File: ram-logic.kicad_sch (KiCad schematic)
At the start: 17 parts, among them SW1 Button, SW202 Programming Switch, U26 74HCT00, U31 74HCT157

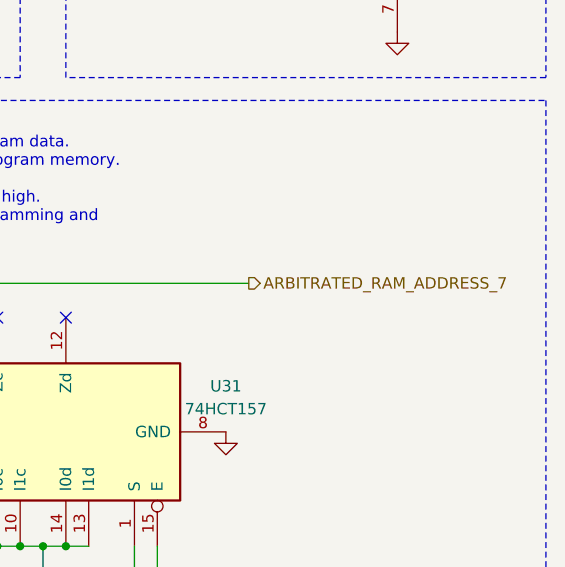
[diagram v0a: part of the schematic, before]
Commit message: ram address 7 led now uses the arbitrated signal
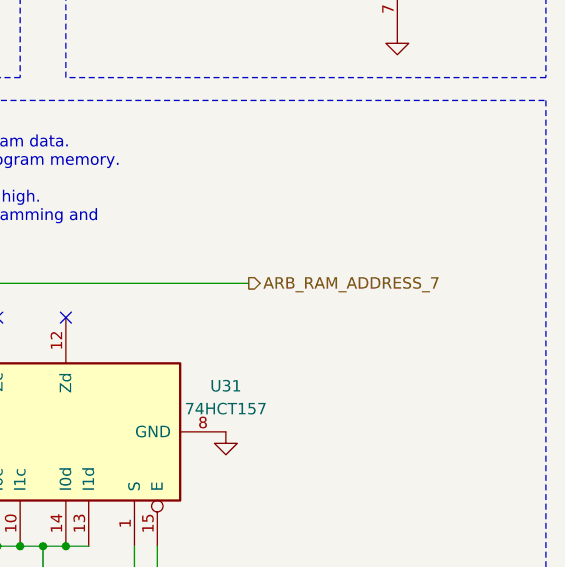
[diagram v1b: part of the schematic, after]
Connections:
- net ARBITRATED_RAM_ADDRESS_7 renamed ARB_RAM_ADDRESS_7
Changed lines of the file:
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@@
     (effects (font (size 1.27 1.27)) (justify left))
   )
-  (hierarchical_label "ARBITRATED_RAM_ADDRESS_7" (shape output) (at 246.38 77.47 0) (fields_autoplaced)
+  (hierarchical_label "ARB_RAM_ADDRESS_7" (shape output) (at 246.38 77.47 0) (fields_autoplaced)
     (effects (font (size 1.27 1.27)) (justify left))
   )

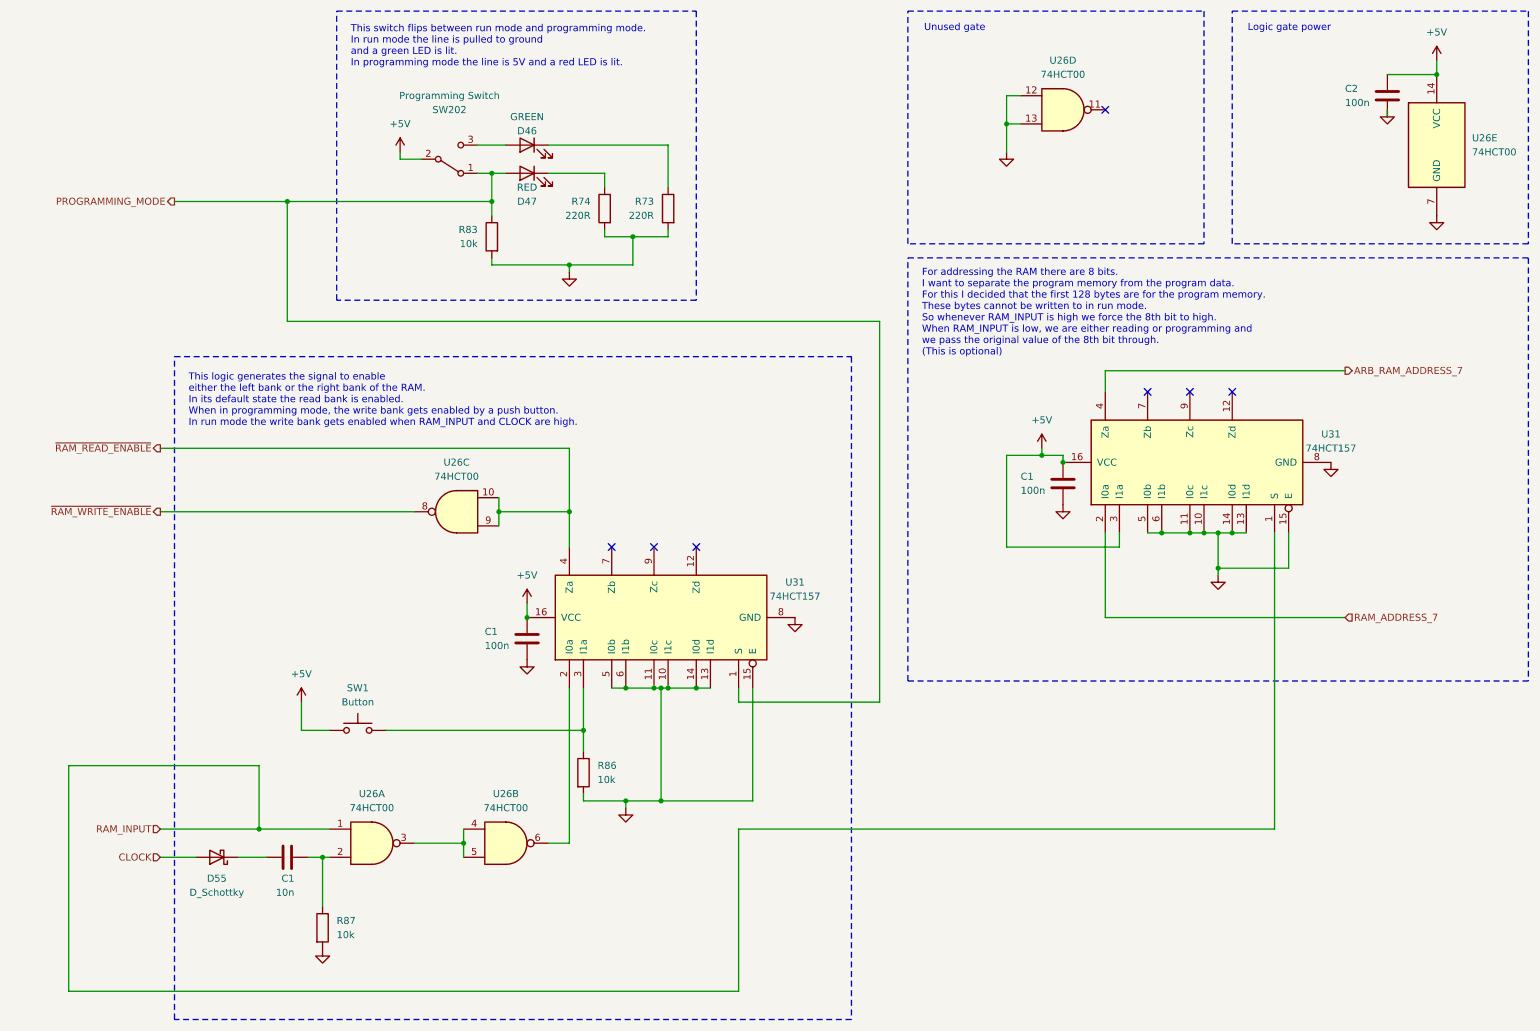
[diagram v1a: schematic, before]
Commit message: added stack and x register.  Added logic for stack_address so ram address 7 gets passes and ram address 8 is high
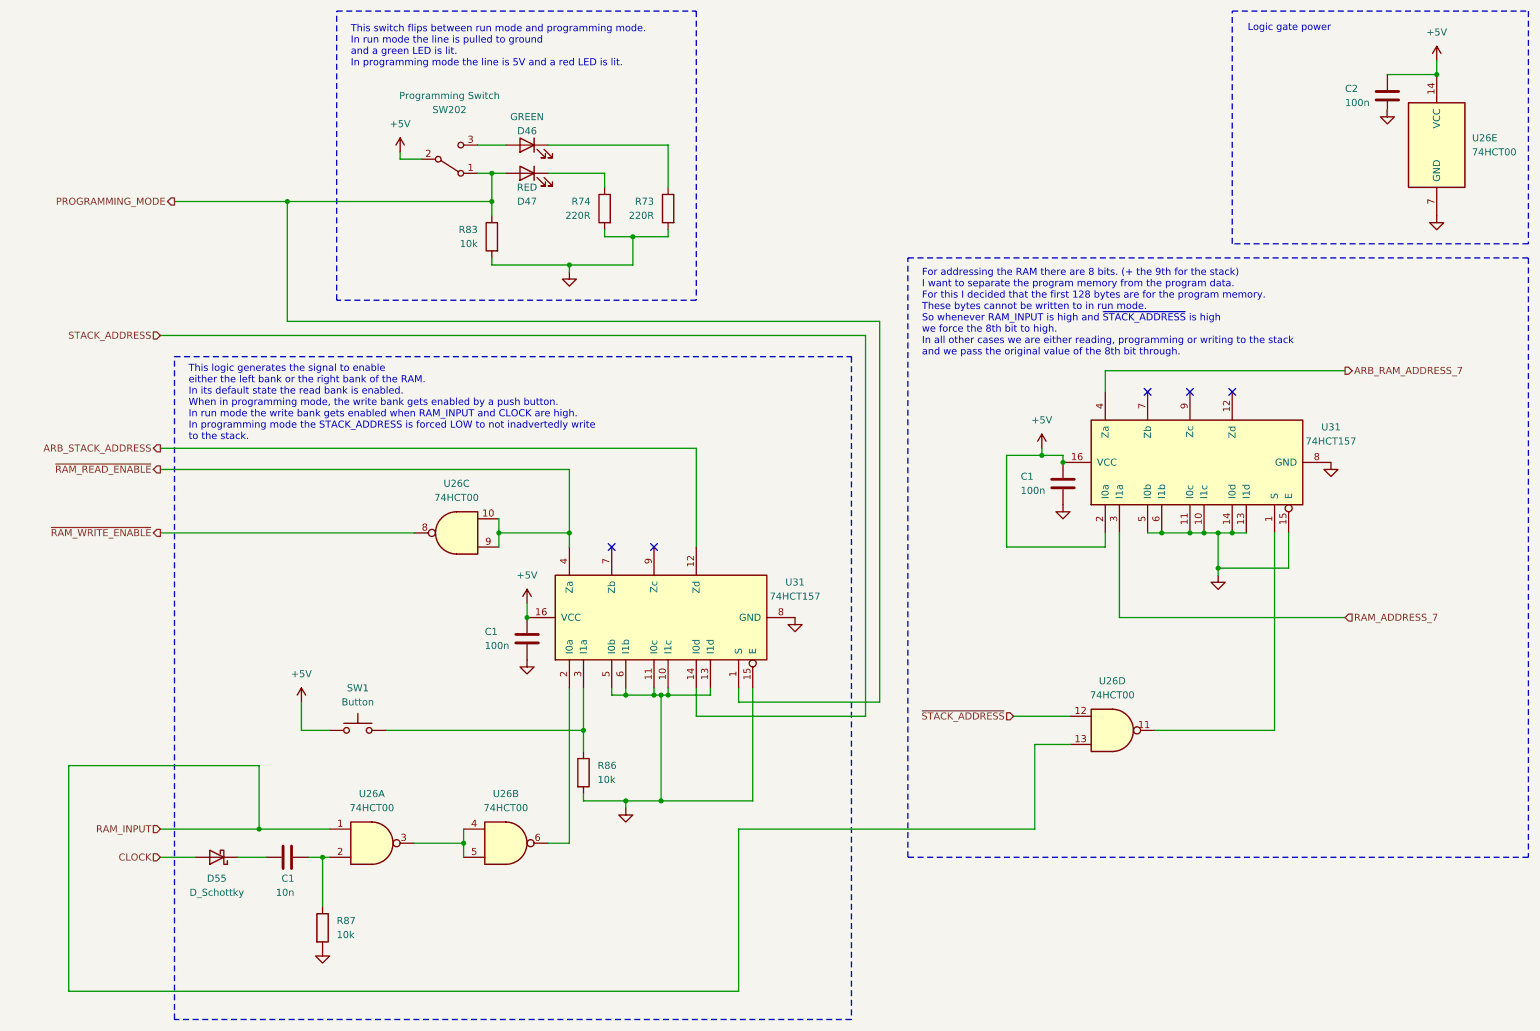
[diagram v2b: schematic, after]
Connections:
- net +5V: now also U31.2 (I0a); no longer U31.3 (I1a)
- net GND: no longer U26.12, U26.13, U31.14 (I0d)
- net RAM_ADDRESS_7: now also U31.3 (I1a); no longer U31.2 (I0a)
- net RAM_INPUT: now also U26.13; no longer U31.1 (S)
- net at U26.11: now also U31.1 (S)
- net ARB_STACK_ADDRESS: now reaches U31.12 (Zd)
- new net STACK_ADDRESS: U31.14 (I0d)
- new net ~{STACK_ADDRESS}: U26.12
- no-connect marks 7 -> 5
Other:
- note added: "For addressing the RAM there are 8 bits. (+ the 9th for the stack) I want to separate the program memory from the program data. For this I decided that the first 128 bytes are for the program memory. These bytes cannot be written to in run mode. So whenever RAM_INPUT is high and ~{STACK_ADDRESS} is high we force the 8th bit to high. In all other cases we are either reading, programming or writing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"
- note added: "This logic generates the signal to enable either the left bank or the right bank of the RAM. In its default state the read bank is enabled. When in programming mode, the write bank gets enabled by a push button. In run mode the write bank gets enabled when RAM_INPUT and CLOCK are high. In programming mode the STACK_ADDRESS is forced LOW to not inadvertedly write to the stack."
- note removed: "For addressing the RAM there are 8 bits. I want to separate the program memory from the program data. For this I decided that the first 128 bytes are for the program memory. These bytes cannot be written to in run mode. So whenever RAM_INPUT is high we force the 8th bit to high. When RAM_INPUT is low, we are either reading or programming and we pass the original value of the 8th bit through. (Thi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"
- note removed: "This logic generates the signal to enable either the left bank or the right bank of the RAM. In its default state the read bank is enabled. When in programming mode, the write bank gets enabled by a push button. In run mode the write bank gets enabled when RAM_INPUT and CLOCK are high."
- note removed: "Unused gate"
- moved on the sheet: U26C

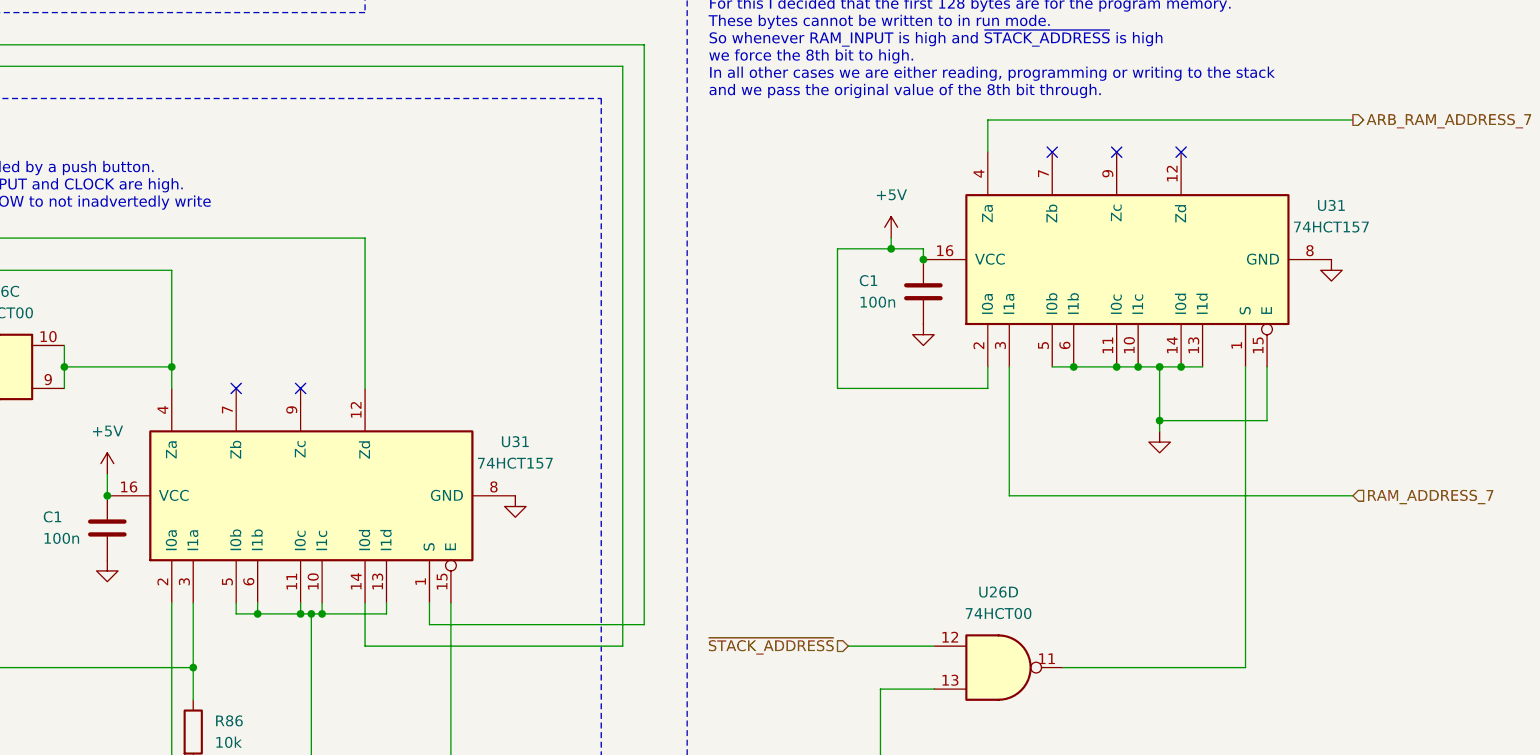
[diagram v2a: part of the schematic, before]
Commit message: changed symbols
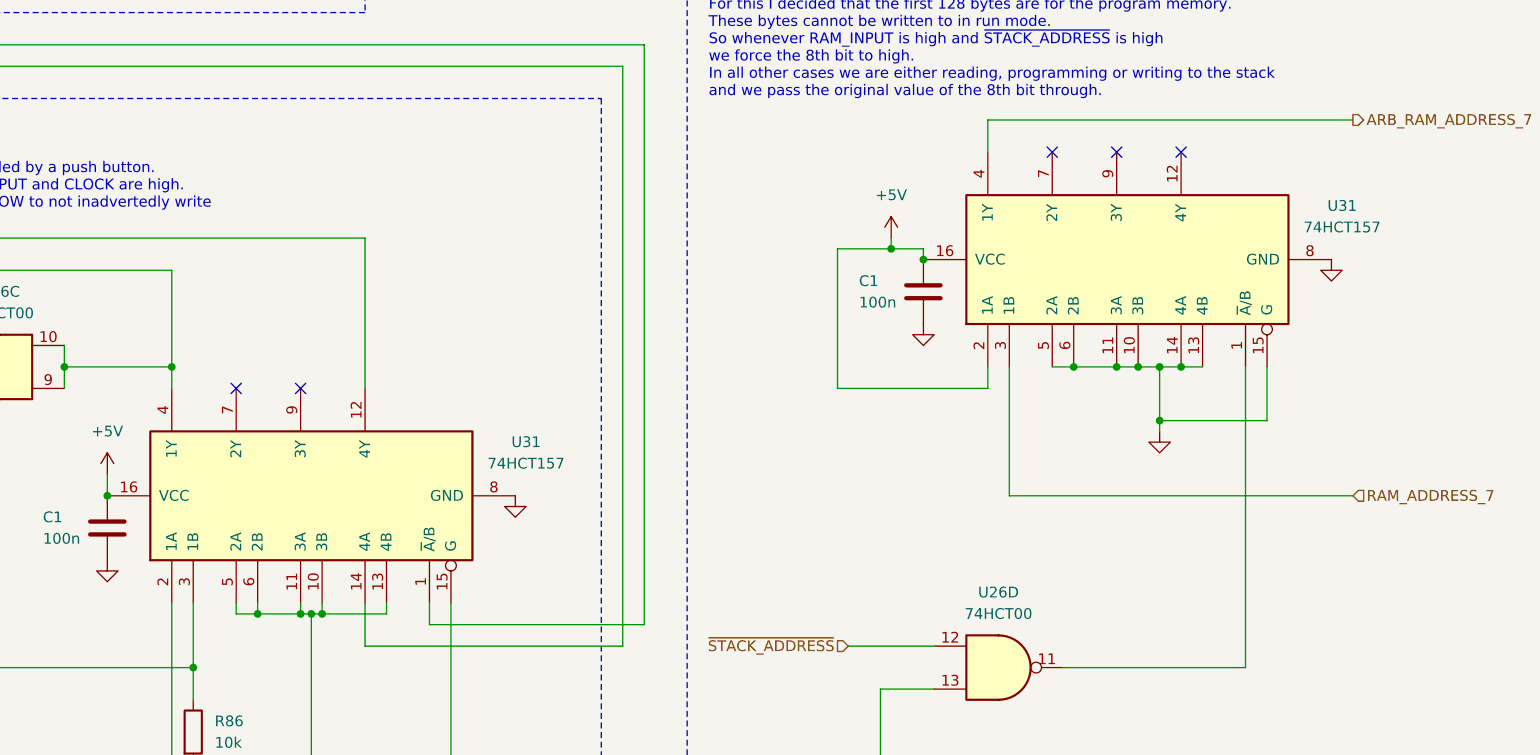
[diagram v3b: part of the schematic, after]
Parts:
- U31: symbol 74xx:74LS157 -> 01_my_library:74HCT157
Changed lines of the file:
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@@
     )
   )
-  (symbol (lib_id "74xx:74LS157") (at 121.92 121.92 90) (unit 1)
+  (symbol (lib_id "01_my_library:74HCT157") (at 123.19 121.92 90) (unit 1)
     (in_bom yes) (on_board yes) (dnp no)
-    (property "Reference" "U31" (at 147.32 115.57 90)
-      (effects (font (size 1.27 1.27)))
-    )
-    (property "Value" "74HCT157" (at 147.32 118.11 90)
-      (effects (font (size 1.27 1.27)))
-    )
-    (property "Footprint" "Package_DIP:DIP-16_W7.62mm" (at 121.92 121.92 0)
-      (effects (font (size 1.27 1.27)) hide)
-    )
-    (property "Datasheet" "http://www.ti.com/lit/gpn/sn74LS157" (at 121.92 121.92 0)
+    (property "Reference" "U31" (at 148.59 115.57 90)
+      (effects (font (size 1.27 1.27)))
+    )
+    (property "Value" "74HCT157" (at 148.59 118.11 90)
+      (effects (font (size 1.27 1.27)))
+    )
+    (property "Footprint" "Package_DIP:DIP-16_W7.62mm" (at 123.19 120.65 0)
+      (effects (font (size 1.27 1.27)) hide)
+    )
+    (property "Datasheet" "https://www.ti.com/lit/ds/symlink/sn74hct157.pdf" (at 158.75 120.65 0)
       (effects (font (size 1.27 1.27)) hide)
     )
@@
     )
   )
-  (symbol (lib_id "74xx:74LS157") (at 218.44 93.98 90) (unit 1)
+  (symbol (lib_id "01_my_library:74HCT157") (at 219.71 93.98 90) (unit 1)
     (in_bom yes) (on_board yes) (dnp no)
-    (property "Reference" "U31" (at 243.84 87.63 90)
-      (effects (font (size 1.27 1.27)))
-    )
-    (property "Value" "74HCT157" (at 243.84 90.17 90)
-      (effects (font (size 1.27 1.27)))
-    )
-    (property "Footprint" "Package_DIP:DIP-16_W7.62mm" (at 218.44 93.98 0)
-      (effects (font (size 1.27 1.27)) hide)
-    )
-    (property "Datasheet" "http://www.ti.com/lit/gpn/sn74LS157" (at 218.44 93.98 0)
-      (effects (font (size 1.27 1.27)) hide)
-    )
+    (property "Reference" "U31" (at 245.11 87.63 90)
+      (effects (font (size 1.27 1.27)))
+    )
+    (property "Value" "74HCT157" (at 245.11 90.17 90)
+      (effects (font (size 1.27 1.27)))
+    )
+    (property "Footprint" "Package_DIP:DIP-16_W7.62mm" (at 219.71 92.71 0)
+      (effects (font (size 1.27 1.27)) hide)
+    )
+    (property "Datasheet" "https://www.ti.com/lit/ds/symlink/sn74hct157.pdf" (at 255.27 92.71 0)
+      (effects (font (size 1.27 1.27)) hide)
+    )
